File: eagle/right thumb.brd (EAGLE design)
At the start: 41.9 x 43 mm, 12 parts, among them J1 B7B-ZR_(LF)(SN)

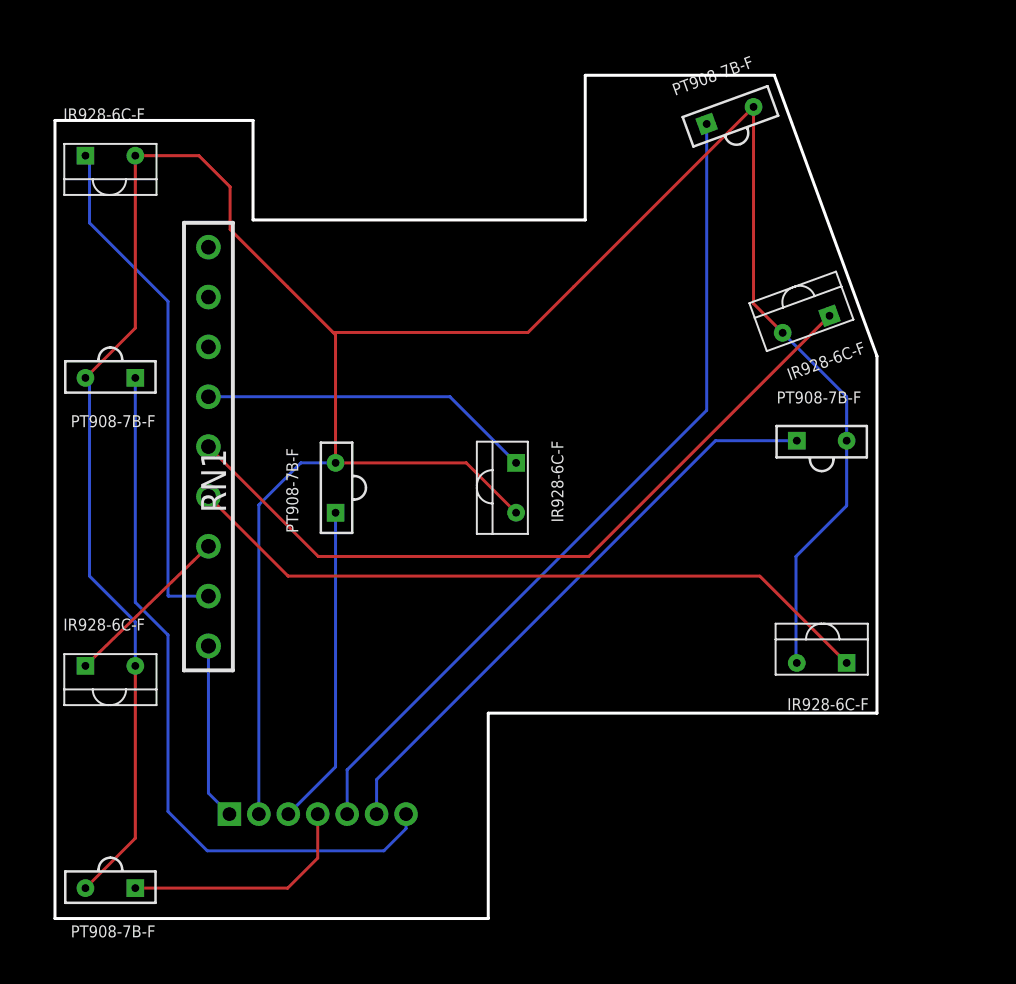
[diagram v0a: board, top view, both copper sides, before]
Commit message: Reduce drill size of resistor holes. Fix right thumb cluster
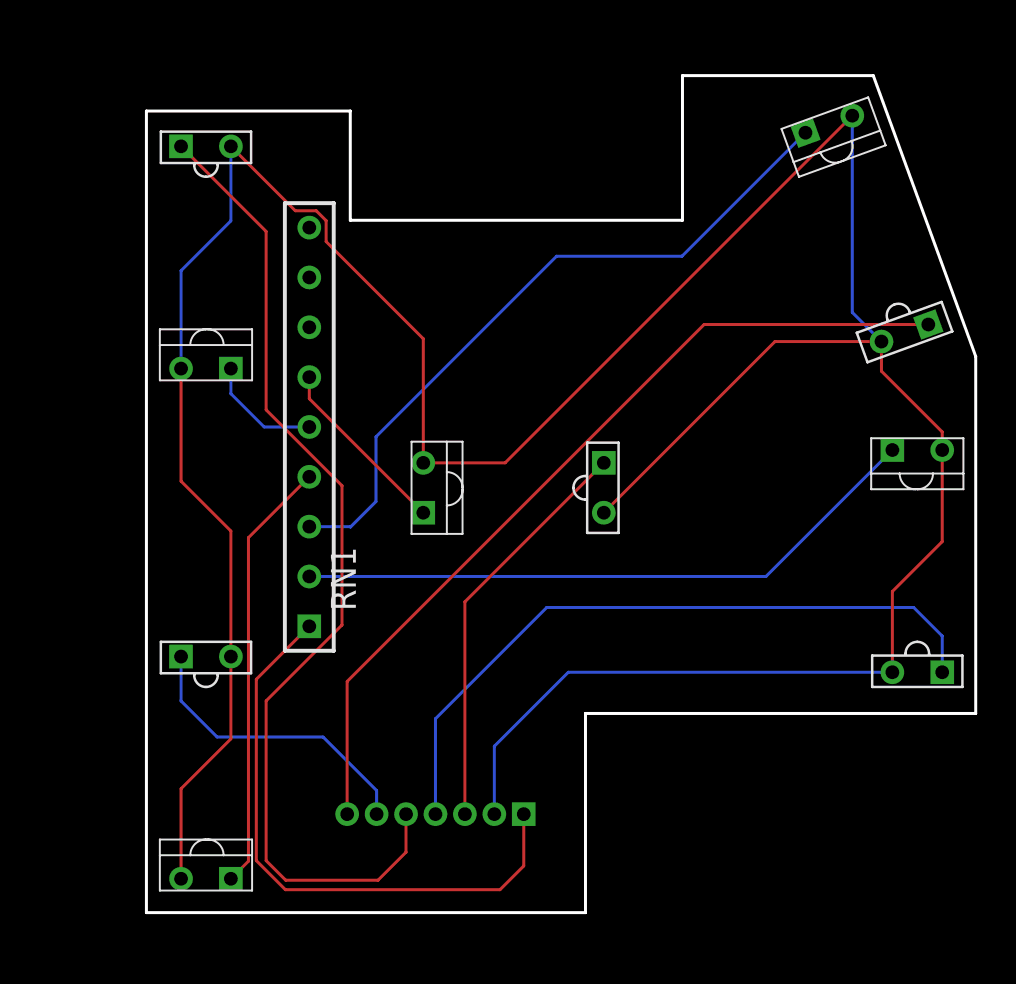
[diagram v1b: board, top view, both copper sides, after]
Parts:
- RN1: value 4309R-101-202LF -> 150R; device 4309R-101-202LF:4309R-101 -> 9 pin resistor network:9PIN-RESISTOR-NETWORK
- moved LED4 42.6 mm to (44.2, 24.4)
- moved PT4 42.6 mm to (44.2, 13.1)
- moved PT5 40.6 mm to (43.6, 30.4), turned to 200 degrees
- moved LED5 36.7 mm to (39.7, 41.0), turned to 20 degrees
- moved PT3 33.3 mm to (7.93, 13.9)
- moved LED3 33.3 mm to (7.93, 2.58)
- moved LED2 30.7 mm to (7.93, 28.6), turned to 180 degrees
- moved PT2 26.8 mm to (7.93, 39.9), turned to 0 degrees
- moved J1 15.0 mm to (24.1, 5.87), turned to 0 degrees
- moved PT1 13.7 mm to (28.2, 22.5), turned to 270 degrees
- moved RN1 5.24 mm to (13.2, 15.4)
- moved LED1 4.73 mm to (19.0, 22.5), turned to 90 degrees
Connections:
- net N$2: now also RN1.3; no longer RN1.2
- net N$3: now also RN1.2; no longer RN1.3
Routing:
- net N$5: track 39.1 -> 5.98 mm
- net N$3: track 8.74 -> 32.4 mm
- net N$8: track 12.2 -> 35.5 mm
- net N$1: track 9.01 -> 30.4 mm
- net N$9: track 30.3 -> 15.3 mm
- net N$7: track 150.8 -> 164.9 mm
- net N$4: track 36.0 -> 22.1 mm
- net N$2: track 26.2 -> 35.7 mm
- net N$10: track 42.8 -> 51.5 mm
- net N$6: track 17.1 -> 9.32 mm
- net N$11: track 37.0 -> 43.9 mm
- net N$12: track 16.4 -> 20.8 mm
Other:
- board size 41.9 x 43 mm -> 42.3 x 42.7 mm
